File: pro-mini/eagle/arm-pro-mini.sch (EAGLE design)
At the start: 61 parts, among them J1 MICRO USB, J2 SWD HEADER, Q1 12Mhz, T1 MMBT3906, U1 PRTR5V0U2X, U2 MIC5225-3.3v, U3 LPC11U35FHI33/501, U4 BAS40-05

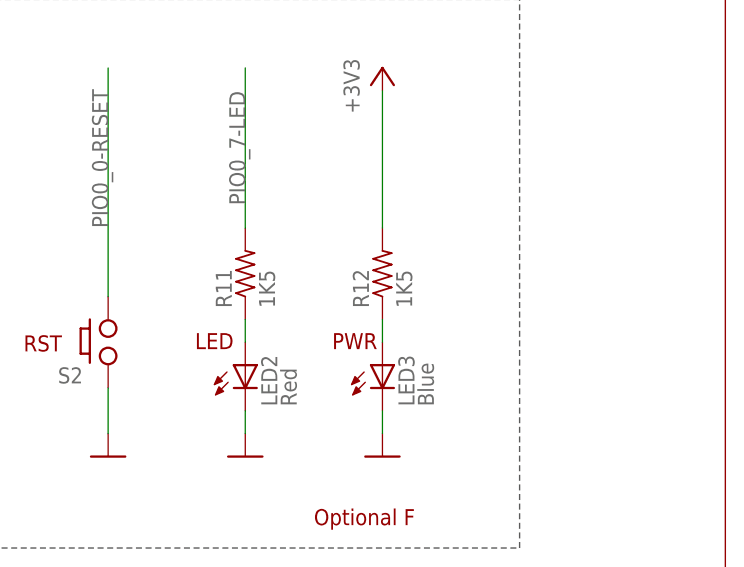
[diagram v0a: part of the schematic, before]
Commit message: Change the value of R12 (blue led) from 1.5k to 10k. It was too bright.
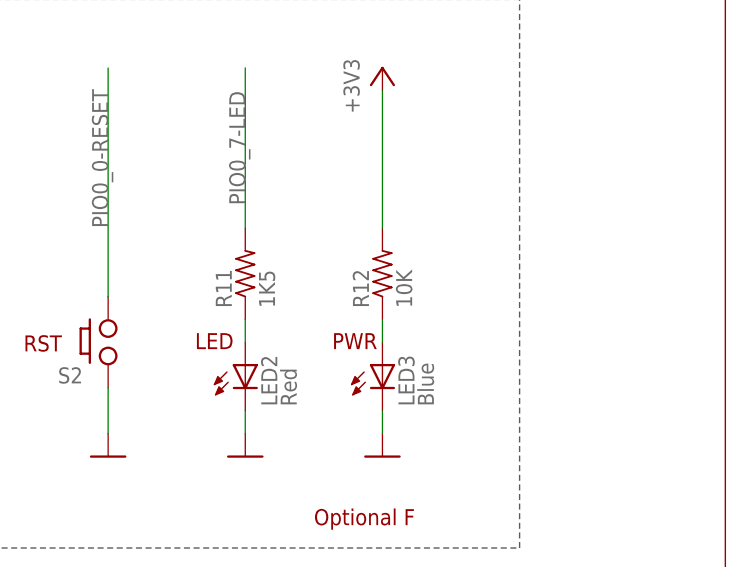
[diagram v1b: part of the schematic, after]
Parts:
- R12: value 1K5 -> 10K
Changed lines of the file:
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@@
 <part name="R3" library="arm-pro-mini" deviceset="R-US_" device="R0402" value="1K5"/>
 <part name="LED3" library="arm-pro-mini" deviceset="LED" device="CHIP-LED0603" value="Blue"/>
-<part name="R12" library="arm-pro-mini" deviceset="R-US_" device="R0402" value="1K5"/>
+<part name="R12" library="arm-pro-mini" deviceset="R-US_" device="R0402" value="10K"/>
 <part name="GND5" library="arm-pro-mini" deviceset="GND" device=""/>
 <part name="R11" library="arm-pro-mini" deviceset="R-US_" device="R0402" value="1K5"/>

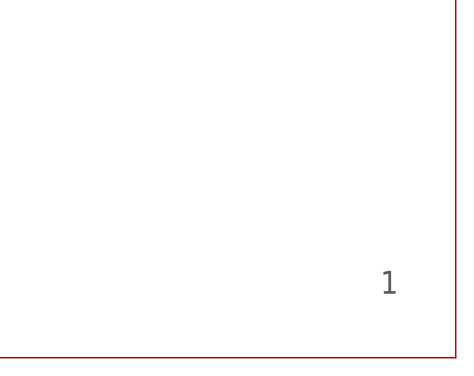
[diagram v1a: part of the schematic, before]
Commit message: Fixed location of RST and ISP switches labels (were swapped in the layout). Added labels for GND, 5V and 3V3 pins. No semantic change. Made the gerber files obsolete. Will generate new ones.
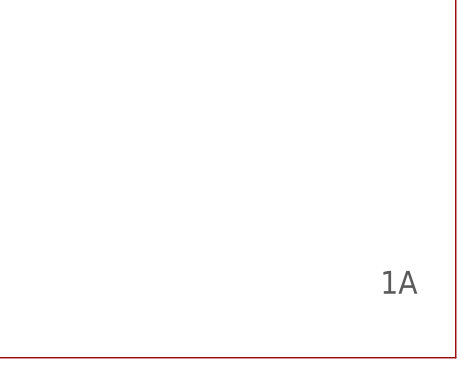
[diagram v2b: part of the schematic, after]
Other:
- note added: "1A"
- note removed: "1"
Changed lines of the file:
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@@
 <wire x1="0" y1="0" x2="0" y2="259.08" width="0.1524" layer="94"/>
 <text x="226.06" y="137.16" size="2.54" layer="97">MCU</text>
-<text x="331.978" y="7.112" size="2.54" layer="97">1</text>
+<text x="331.978" y="7.112" size="2.54" layer="97">1A</text>
 <text x="73.914" y="30.48" size="2.54" layer="97">3.3V REGULATOR</text>
 <text x="66.04" y="124.46" size="2.54" layer="97">USB</text>

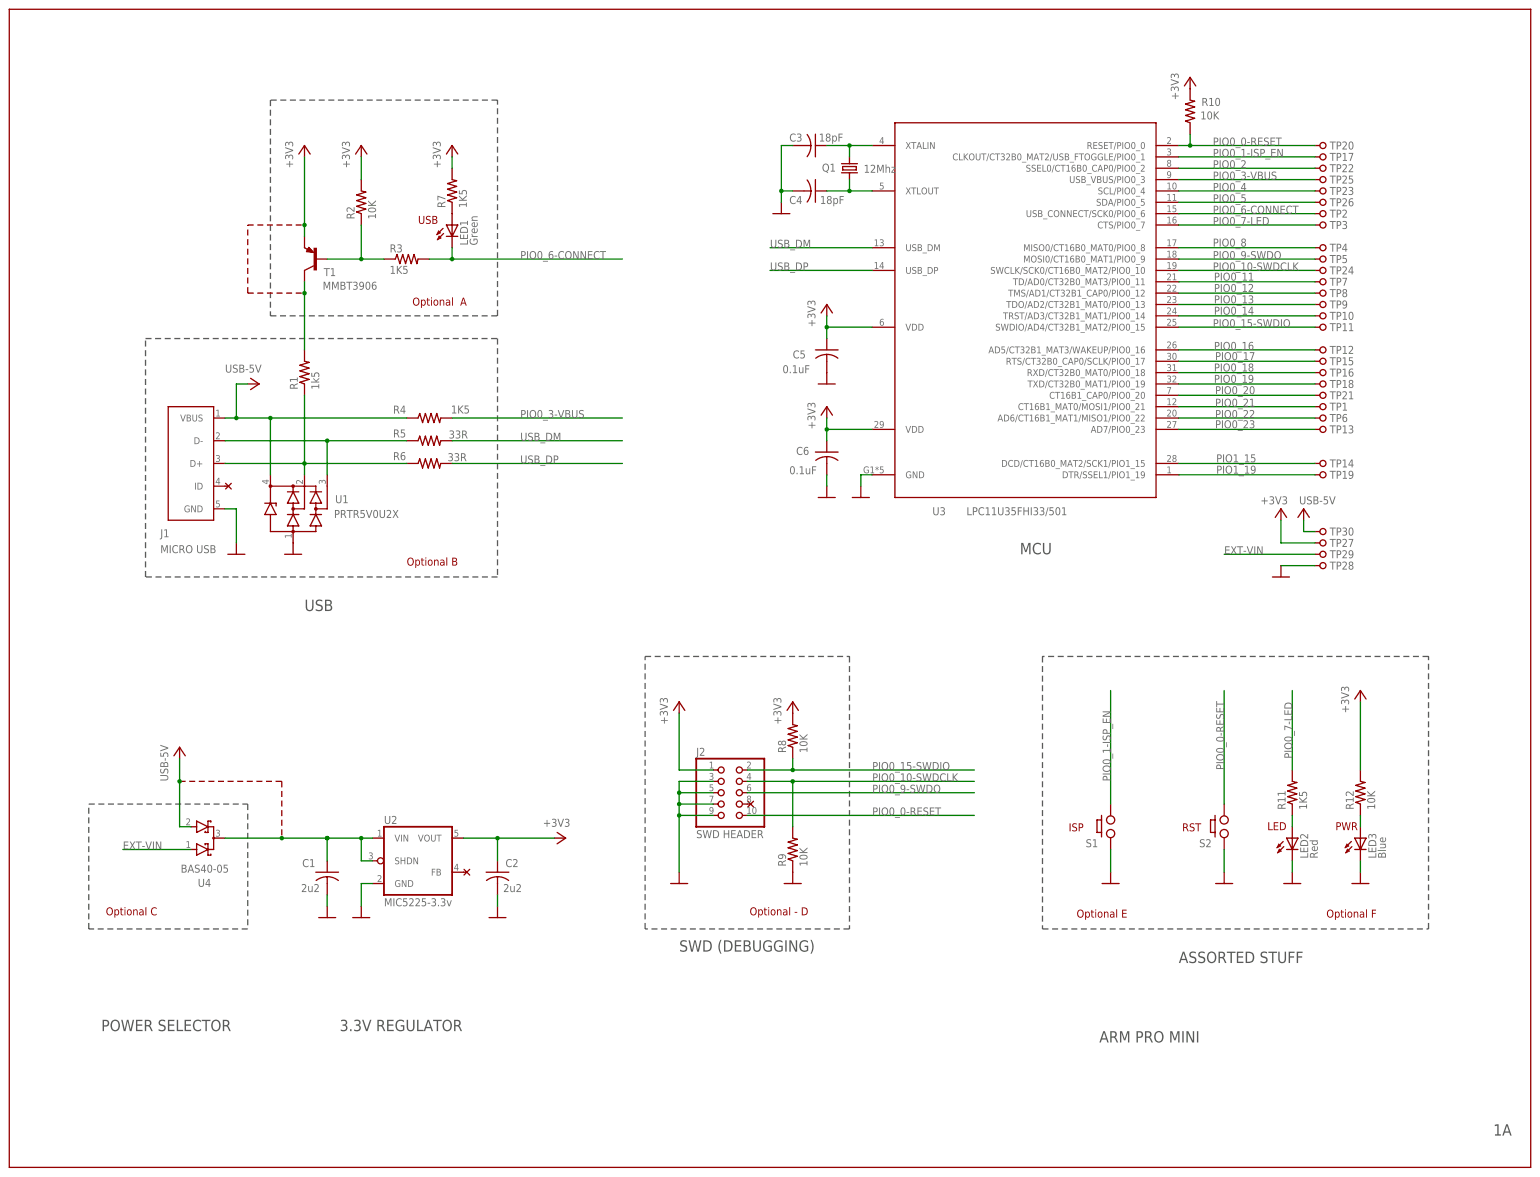
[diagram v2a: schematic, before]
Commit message: Tweaked the schematic, no semantic change.
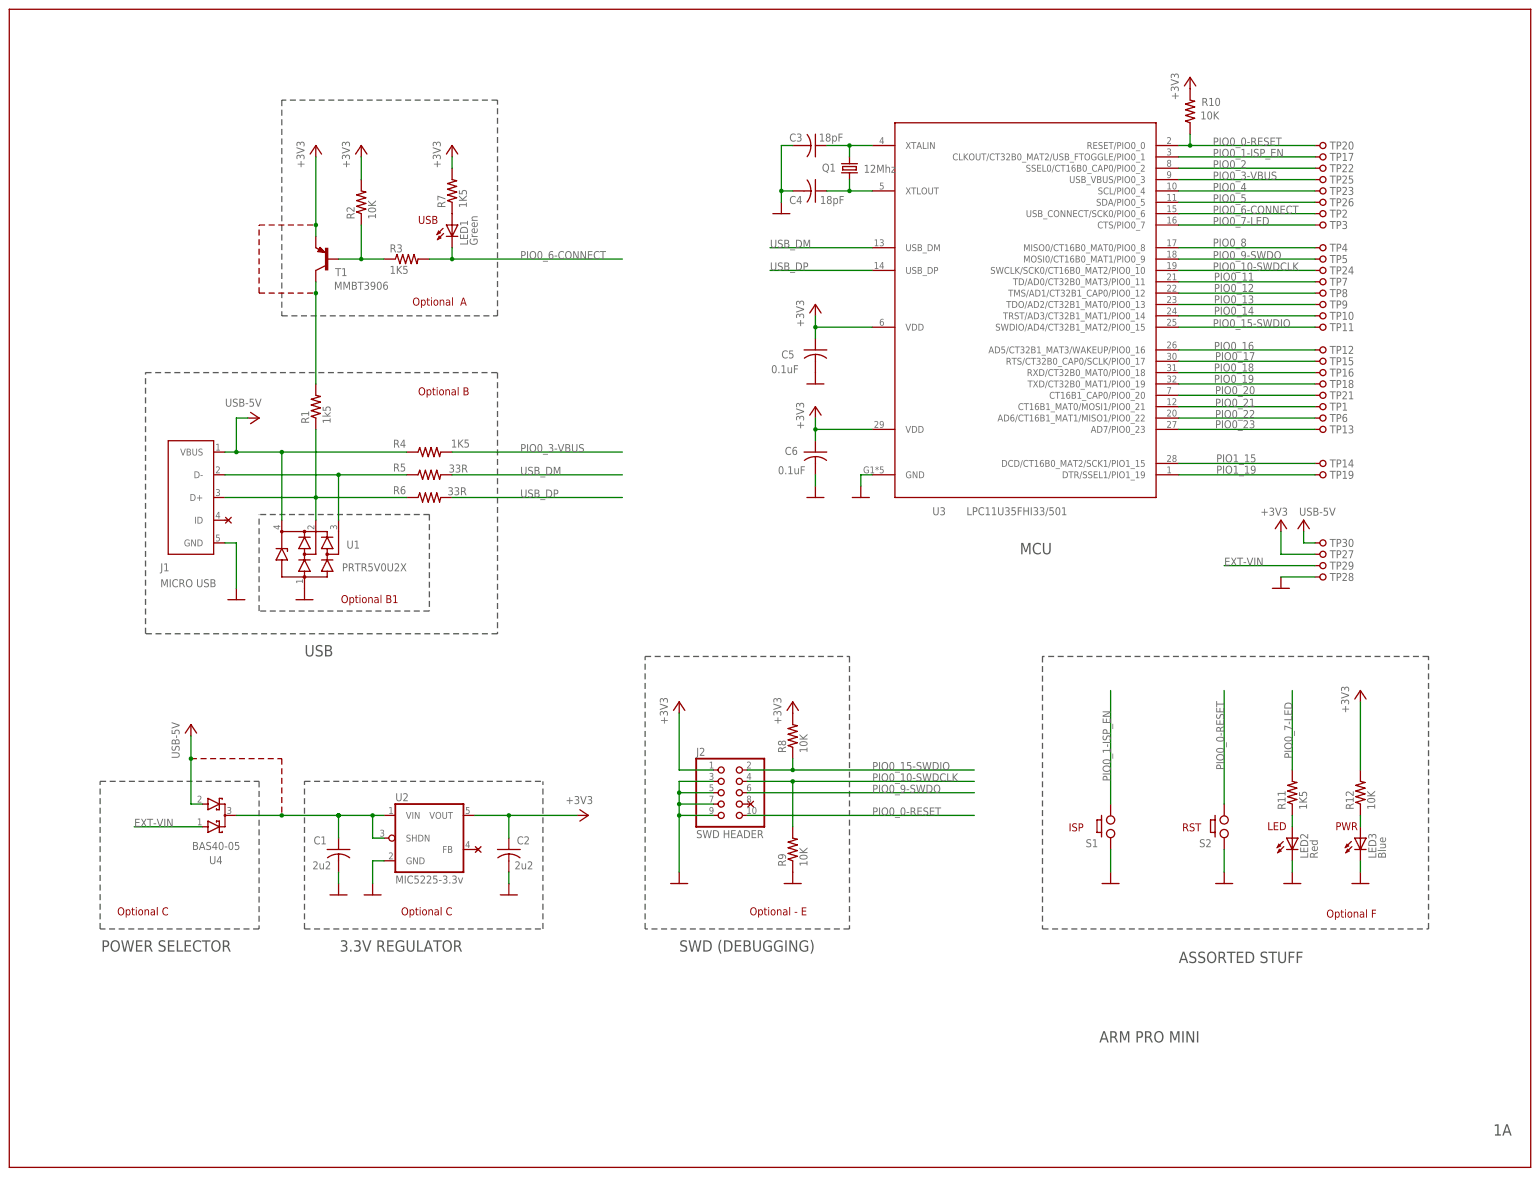
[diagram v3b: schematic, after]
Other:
- note added: "Optional - E"
- note added: "Optional B1"
- note removed: "Optional - D"
- note removed: "Optional E"
- moved on the sheet: C1, C2, C5, C6, J1, R1, R4, R5, R6, T1, TP27, TP28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
